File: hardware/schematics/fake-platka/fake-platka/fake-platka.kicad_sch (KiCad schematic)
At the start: 3 parts

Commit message: starting to write the documentation
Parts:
- removed U? (x2): TB67H450AFNG_EL, P-HSOP8-0405-1.27-002_TOS, symbol library:TB67H450AFNG_EL
- gave numbers to parts that had none: 1

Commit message: made first pcb
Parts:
- removed U1: SC0915-pico-w-board, SC0915_RPI, symbol library:SC0915-pico-w-board
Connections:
- no-connect marks 0 -> 8
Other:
- removed sheet leg-electronics
- added sheet Left Controller  (left_controller.kicad_sch)
- added sheet Leg Back Left (leg_bl.kicad_sch)
- added sheet Leg Back Right (leg_br.kicad_sch)
- added sheet Leg Fornt Left (leg_fl.kicad_sch)
- added sheet Leg Front Right (leg_fr.kicad_sch)
- added sheet Power Supply (power_supply.kicad_sch)
- added sheet Right Controller (right_controller.kicad_sch)

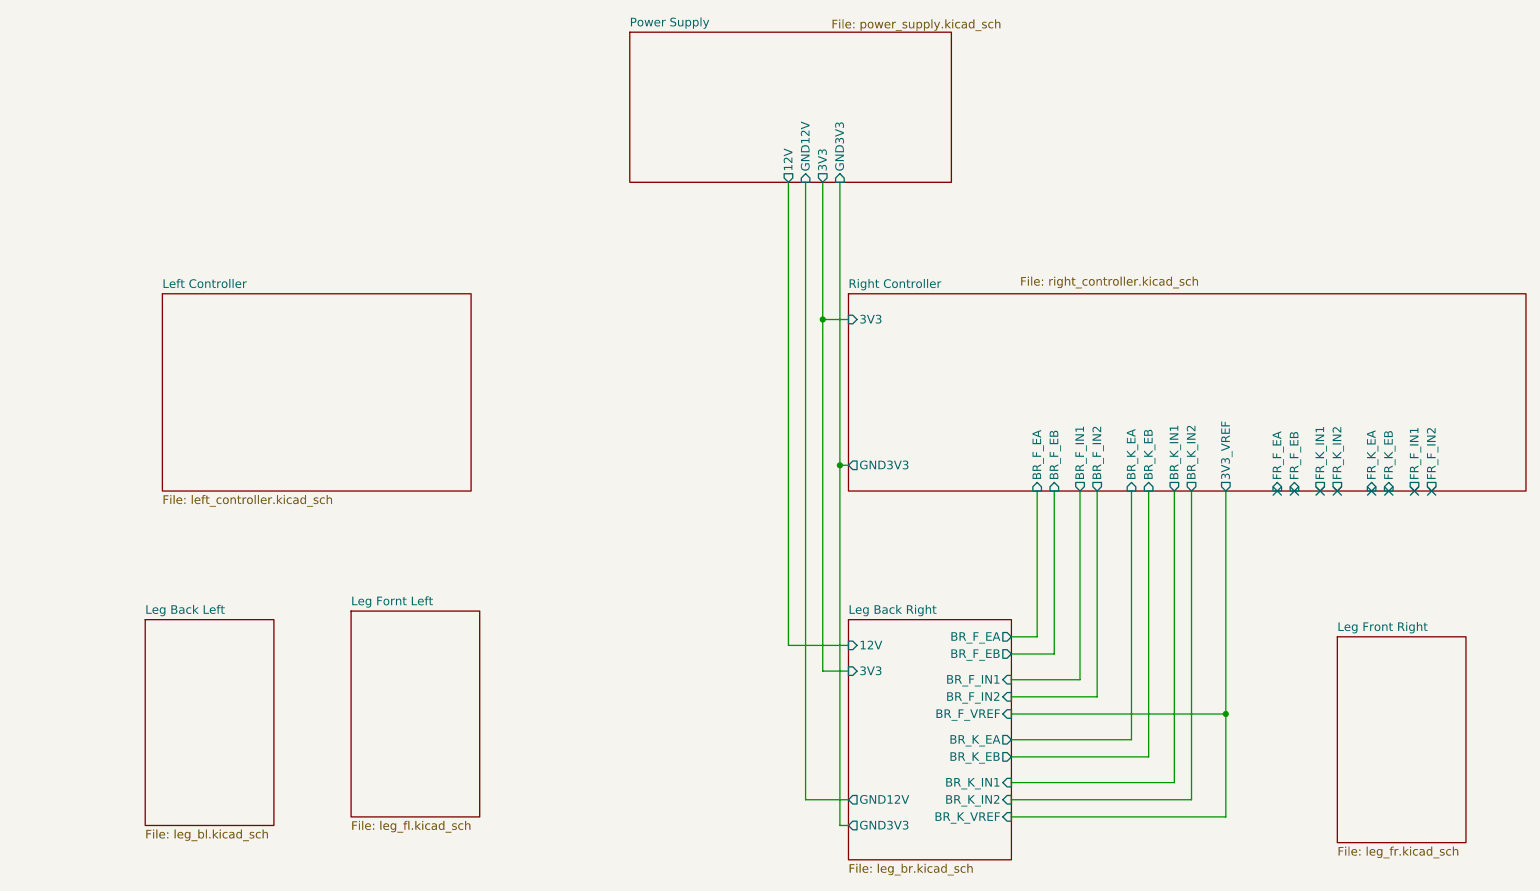
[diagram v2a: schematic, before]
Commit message: added all components to the schematic and pcb
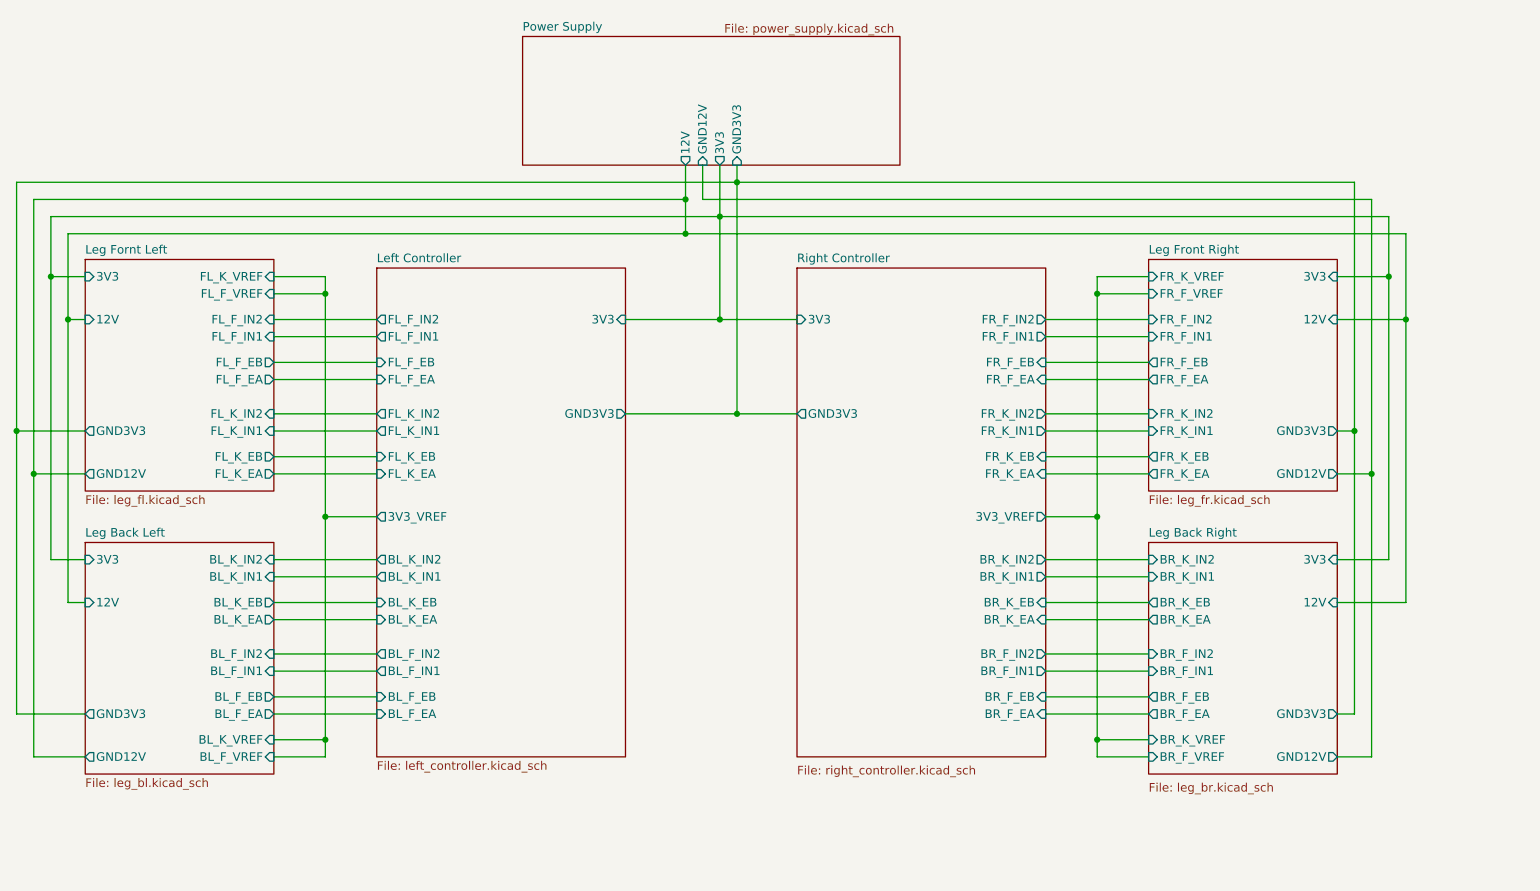
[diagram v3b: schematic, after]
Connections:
- no-connect marks 8 -> 0
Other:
- sheet Left Controller  ports: added 3V3, 3V3_VREF, BL_F_EA, BL_F_EB, BL_F_IN1, BL_F_IN2, BL_K_EA, BL_K_EB, BL_K_IN1, BL_K_IN2, FL_F_EA, FL_F_EB, FL_F_IN1, FL_F_IN2, FL_K_EA, FL_K_EB, FL_K_IN1, FL_K_IN2, GND3V3; removed none
- sheet Leg Back Left ports: added 12V, 3V3, BL_F_EA, BL_F_EB, BL_F_IN1, BL_F_IN2, BL_F_VREF, BL_K_EA, BL_K_EB, BL_K_IN1, BL_K_IN2, BL_K_VREF, GND12V, GND3V3; removed none
- sheet Leg Fornt Left ports: added 12V, 3V3, FL_F_EA, FL_F_EB, FL_F_IN1, FL_F_IN2, FL_F_VREF, FL_K_EA, FL_K_EB, FL_K_IN1, FL_K_IN2, FL_K_VREF, GND12V, GND3V3; removed none
- sheet Leg Front Right ports: added 12V, 3V3, FR_F_EA, FR_F_EB, FR_F_IN1, FR_F_IN2, FR_F_VREF, FR_K_EA, FR_K_EB, FR_K_IN1, FR_K_IN2, FR_K_VREF, GND12V, GND3V3; removed none

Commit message: working on pcb and documentation
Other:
- company: (none) -> By Andrey Shefa
- title: (none) -> First pcb for quadruped robot v3
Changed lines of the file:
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@@
 (kicad_sch (version 20211123) (generator eeschema)
   (paper "A4")
+  (title_block
+    (title "First pcb for quadruped robot v3")
+    (date "2024-02-06")
+    (rev "0")
+    (company "By Andrey Shefa")
+  )
   (junction (at 243.84 86.36) (diameter 0) (color 0 0 0 0)
   )
@@
       (reference "J4") (unit 1) (value "B2B-EH-A") (footprint "quadruped-lib-footprints:CONN_B2B-EH-A LFSN_JST")
     )
-    (path "/62b0d172-d9b2-4e28-b0b7-ce687b217478/c9005eb5-6888-44be-895a-94ca89765e9e"
+    (path "/62b0d172-d9b2-4e28-b0b7-ce687b217478/c94ff8b0-3cd3-4943-a7e9-95656222931c"
       (reference "J5") (unit 1) (value "B2B-EH-A") (footprint "quadruped-lib-footprints:CONN_B2B-EH-A LFSN_JST")
     )
@@
       (reference "J11") (unit 1) (value "B2B-EH-A") (footprint "quadruped-lib-footprints:CONN_B2B-EH-A LFSN_JST")
     )
-    (path "/b9729da1-83cd-46e4-9640-46cc1799dcb8/a81d3b16-a6aa-41a6-b00e-67cb06b3cb7d"
+    (path "/b9729da1-83cd-46e4-9640-46cc1799dcb8/1c0f6c01-adfc-4c4a-9d3b-2fc74a2062a4"
       (reference "J12") (unit 1) (value "B2B-EH-A") (footprint "quadruped-lib-footprints:CONN_B2B-EH-A LFSN_JST")
     )
@@
       (reference "J18") (unit 1) (value "B2B-EH-A") (footprint "quadruped-lib-footprints:CONN_B2B-EH-A LFSN_JST")
     )
-    (path "/79f7bb11-13c3-435a-b9d5-e1cf9480adeb/9ef99685-0bca-481b-9e69-640861986b4a"
+    (path "/79f7bb11-13c3-435a-b9d5-e1cf9480adeb/1fabcd83-df40-4d26-844f-63aa0ae1c4a1"
       (reference "J19") (unit 1) (value "B2B-EH-A") (footprint "quadruped-lib-footprints:CONN_B2B-EH-A LFSN_JST")
     )
@@
       (reference "J25") (unit 1) (value "B2B-EH-A") (footprint "quadruped-lib-footprints:CONN_B2B-EH-A LFSN_JST")
     )
-    (path "/5b44027f-780b-461c-ac9a-c4fccf41f116/2494c4d4-65e2-462b-9b63-9ecad69af53e"
+    (path "/5b44027f-780b-461c-ac9a-c4fccf41f116/cd631f09-8b89-44a2-a320-da3e07b54a95"
       (reference "J26") (unit 1) (value "B2B-EH-A") (footprint "quadruped-lib-footprints:CONN_B2B-EH-A LFSN_JST")
     )
@@
       (reference "R4") (unit 1) (value "5K") (footprint "Resistor_THT:R_Axial_DIN0207_L6.3mm_D2.5mm_P10.16mm_Horizontal")
     )
-    (path "/62b0d172-d9b2-4e28-b0b7-ce687b217478/6ac3e022-3370-4440-ad90-896845020c26"
+    (path "/62b0d172-d9b2-4e28-b0b7-ce687b217478/22e5db91-302a-4f7d-8f54-6bee881fc29a"
       (reference "R5") (unit 1) (value "150R") (footprint "Resistor_THT:R_Axial_DIN0207_L6.3mm_D2.5mm_P10.16mm_Horizontal")
     )
@@
       (reference "R13") (unit 1) (value "5K") (footprint "Resistor_THT:R_Axial_DIN0207_L6.3mm_D2.5mm_P10.16mm_Horizontal")
     )
-    (path "/b9729da1-83cd-46e4-9640-46cc1799dcb8/746f9e15-8287-48b7-ba7e-d41f125888f3"
+    (path "/b9729da1-83cd-46e4-9640-46cc1799dcb8/f99d87d1-2b02-4f25-a04b-de2660fbf270"
       (reference "R14") (unit 1) (value "150R") (footprint "Resistor_THT:R_Axial_DIN0207_L6.3mm_D2.5mm_P10.16mm_Horizontal")
     )
@@
       (reference "R22") (unit 1) (value "5K") (footprint "Resistor_THT:R_Axial_DIN0207_L6.3mm_D2.5mm_P10.16mm_Horizontal")
     )
-    (path "/79f7bb11-13c3-435a-b9d5-e1cf9480adeb/6f2f92f7-1a1d-46a8-b2ee-3a54f42b9979"
+    (path "/79f7bb11-13c3-435a-b9d5-e1cf9480adeb/3ba21b93-41e4-4b7c-9eed-1b381845351f"
       (reference "R23") (unit 1) (value "150R") (footprint "Resistor_THT:R_Axial_DIN0207_L6.3mm_D2.5mm_P10.16mm_Horizontal")
     )
@@
       (reference "R31") (unit 1) (value "5K") (footprint "Resistor_THT:R_Axial_DIN0207_L6.3mm_D2.5mm_P10.16mm_Horizontal")
     )
-    (path "/5b44027f-780b-461c-ac9a-c4fccf41f116/a5a2a0ba-6c48-4895-b180-a74d8619e334"
+    (path "/5b44027f-780b-461c-ac9a-c4fccf41f116/789e2e1a-2b2f-4ea8-861a-bcd4d295ae3b"
       (reference "R32") (unit 1) (value "150R") (footprint "Resistor_THT:R_Axial_DIN0207_L6.3mm_D2.5mm_P10.16mm_Horizontal")
     )
